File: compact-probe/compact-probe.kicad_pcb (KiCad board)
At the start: 2 copper layers, 47.5 x 47.5 mm, 27 parts, among them IC1 ATA6561-GBQW-N, J1 Conn_01x08_Male, J2 Conn_01x04_Male, J3 Conn_02x05_Odd_Even, J4 Conn_01x01_Female, J5 Conn_01x01_Female, J6 Conn_01x01_Female, J7 Conn_01x01_Female, J8 Conn_01x01_Female, U4 ESP32-C3-WROOM-02-H4, U6 LT1963AxST-3.3

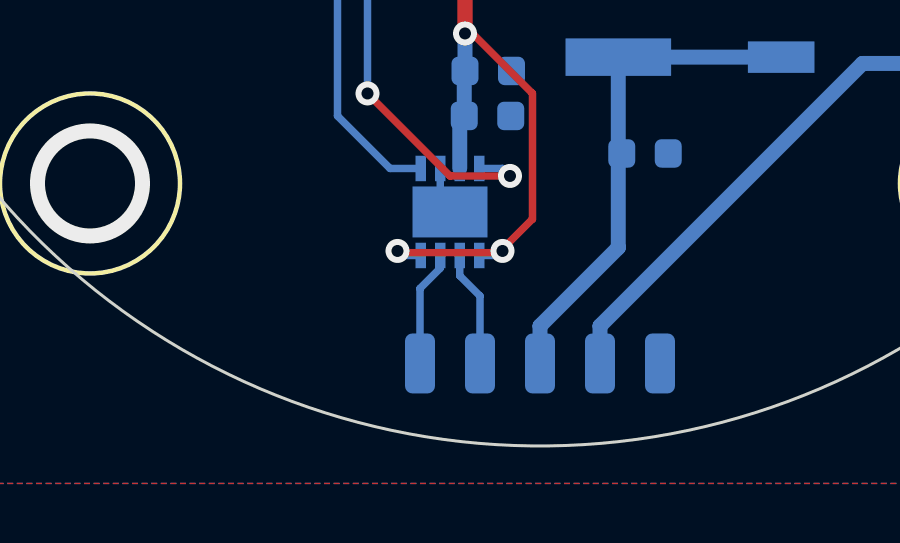
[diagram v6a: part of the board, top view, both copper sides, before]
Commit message: Added CANBus 120 ohm termination resistor.
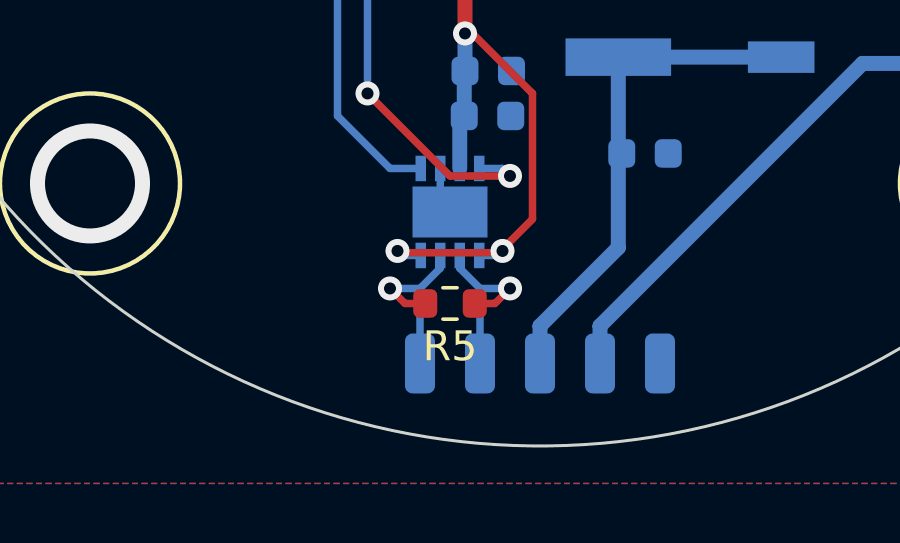
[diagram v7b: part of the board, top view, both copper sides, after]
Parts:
- added R5: 120Ω, Resistor_SMD:R_0603_1608Metric, F.Cu at (-3.00, 19.0)
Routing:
- net CANL: track 3.88 -> 6.26 mm, vias 0 -> 1
- net CANH: track 3.88 -> 6.26 mm, vias 0 -> 1
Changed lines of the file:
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@@
   (net 27 "unconnected-(J3-Pad9)")
   (net 28 "unconnected-(J3-Pad10)")
+  (footprint "Resistor_SMD:R_0603_1608Metric" (layer "F.Cu")
+    (at -3 19 180)
+    (descr "Resistor SMD 0603 (1608 Metric), square (rectangular) end terminal, IPC_7351 nominal, (Body size source: IPC-SM-782 page 72, https://www.pcb-3d.com/wordpress/wp-content/uploads/ipc-sm-782a_amendment_1_and_2.pdf), generated with kicad-footprint-generator")
+    (tags "resistor")
+    (property "Sheetfile" "compact-probe.kicad_sch")
+    (property "Sheetname" "")
+    (attr smd)
+    (fp_text reference "R5" (at 0 -1.43) (layer "F.SilkS")
+      (effects (font (size 1 1) (thickness 0.15)))
+    )
+    (fp_text value "120Ω" (at 0 1.43) (layer "F.Fab")
+      (effects (font (size 1 1) (thickness 0.15)))
+    )
+    (fp_text user "${REFERENCE}" (at 0 0) (layer "F.Fab")
+      (effects (font (size 0.4 0.4) (thickness 0.06)))
+    )
+    (fp_line (start -0.237258 0.5225) (end 0.237258 0.5225) (layer "F.SilkS") (width 0.12))
+    (fp_line (start -0.237258 -0.5225) (end 0.237258 -0.5225) (layer "F.SilkS") (width 0.12))
+    (fp_line (start -1.48 0.73) (end -1.48 -0.73) (layer "F.CrtYd") (width 0.05))
+    (fp_line (start 1.48 0.73) (end -1.48 0.73) (layer "F.CrtYd") (width 0.05))
+    (fp_line (start 1.48 -0.73) (end 1.48 0.73) (layer "F.CrtYd") (width 0.05))
+    (fp_line (start -1.48 -0.73) (end 1.48 -0.73) (layer "F.CrtYd") (width 0.05))
+    (fp_line (start 0.8 0.4125) (end -0.8 0.4125) (layer "F.Fab") (width 0.1))
+    (fp_line (start 0.8 -0.4125) (end 0.8 0.4125) (layer "F.Fab") (width 0.1))
+    (fp_line (start -0.8 -0.4125) (end 0.8 -0.4125) (layer "F.Fab") (width 0.1))
+    (fp_line (start -0.8 0.4125) (end -0.8 -0.4125) (layer "F.Fab") (width 0.1))
+    (pad "1" smd roundrect (at -0.825 0 180) (size 0.8 0.95) (layers "F.Cu" "F.Paste" "F.Mask") (roundrect_rratio 0.25)
+      (net 22 "CANL") (pintype "passive"))
+    (pad "2" smd roundrect (at 0.825 0 180) (size 0.8 0.95) (layers "F.Cu" "F.Paste" "F.Mask") (roundrect_rratio 0.25)
+      (net 21 "CANH") (pintype "passive"))
+    (model "${KICAD6_3DMODEL_DIR}/Resistor_SMD.3dshapes/R_0603_1608Metric.wrl"
+      (offset (xyz 0 0 0))
+      (scale (xyz 1 1 1))
+      (rotate (xyz 0 0 0))
+    )
+  )
   (footprint "LED_SMD:LED_0603_1608Metric" (layer "F.Cu")
     (at -10.25 -19.25 -90)
@@
   (segment (start 2 21) (end 2 19.75) (width 0.5) (layer "B.Cu") (net 20))
   (segment (start 17.8 9.475) (end 17.775 9.5) (width 0.5) (layer "B.Cu") (net 20))
+  (segment (start -4.5 19) (end -5 18.5) (width 0.25) (layer "F.Cu") (net 21))
+  (segment (start -3.825 19) (end -4.5 19) (width 0.25) (layer "F.Cu") (net 21))
+  (via (at -5 18.5) (size 0.8) (drill 0.4) (layers "F.Cu" "B.Cu") (net 21))
+  (segment (start -4 18.5) (end -5 18.5) (width 0.25) (layer "B.Cu") (net 21))
   (segment (start -3.325 17.825) (end -4 18.5) (width 0.25) (layer "B.Cu") (net 21))
   (segment (start -4 18.5) (end -4 21) (width 0.25) (layer "B.Cu") (net 21))
   (segment (start -3.325 17.4) (end -3.325 17.825) (width 0.25) (layer "B.Cu") (net 21))
-  (segment (start -2.675 17.4) (end -2.675 18.075) (width 0.25) (layer "B.Cu") (net 22))
-  (segment (start -2.675 18.075) (end -2 18.75) (width 0.25) (layer "B.Cu") (net 22))
-  (segment (start -2 18.75) (end -2 21) (width 0.25) (layer "B.Cu") (net 22))
+  (segment (start -1 18.5) (end -1.5 19) (width 0.25) (layer "F.Cu") (net 22))
+  (segment (start -1.5 19) (end -2.175 19) (width 0.25) (layer "F.Cu") (net 22))
+  (via (at -1 18.5) (size 0.8) (drill 0.4) (layers "F.Cu" "B.Cu") (net 22))
+  (segment (start -2.675 17.4) (end -2.675 17.825) (width 0.25) (layer "B.Cu") (net 22))
+  (segment (start -2 18.5) (end -1 18.5) (width 0.25) (layer "B.Cu") (net 22))
+  (segment (start -2.675 17.825) (end -2 18.5) (width 0.25) (layer "B.Cu") (net 22))
+  (segment (start -2 18.5) (end -2 21) (width 0.25) (layer "B.Cu") (net 22))
   (segment (start 4.5 -4.5) (end 4.5 -2) (width 0.25) (layer "F.Cu") (net 23))
   (segment (start 7.5 -7.9) (end 7.5 -7.5) (width 0.25) (layer "F.Cu") (net 23))

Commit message: Finished design & created fab outputs.
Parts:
- moved C4 15.3 mm to (-0.90, 1.50)
- moved R1 15.3 mm to (0.85, 1.50)
- moved C5 0.25 mm to (10.5, 1.50)
- moved G*** 0.25 mm to (17.8, -8.00)
- moved G*** 0.25 mm to (-6.25, -18.0)
- moved J2 0.25 mm to (17.8, -2.00)
- moved R2 0.25 mm to (-10.5, -18.8)
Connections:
- J3 pad 7: unconnected-(J3-Pad7) -> VBAT
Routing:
- net VBAT: track 24.0 -> 60.7 mm, vias 0 -> 1
- net +3V3: track 126.2 -> 122.3 mm
- net SDA: track 11.5 -> 12.2 mm
- net GND: vias 5 -> 35
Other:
- board text added: "Airball Compact Probe Copyright © 2023, The Airball authors 2023-03-14"
- board text removed: "Airball Compact Probe Copyright (c) 2023, The Airball authors 2023-03-11"
